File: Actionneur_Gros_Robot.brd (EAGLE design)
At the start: 110 x 55 mm, 51 parts, among them M1 ARDUINO-NANO-3.0, M10 SERVO, M11 SERVO, M2 SERVO, M3 SERVO, M4 SERVO, M5 SERVO, M6 SERVO, M7 SERVO, M8 SERVO, M9 SERVO, Y1 16MHz

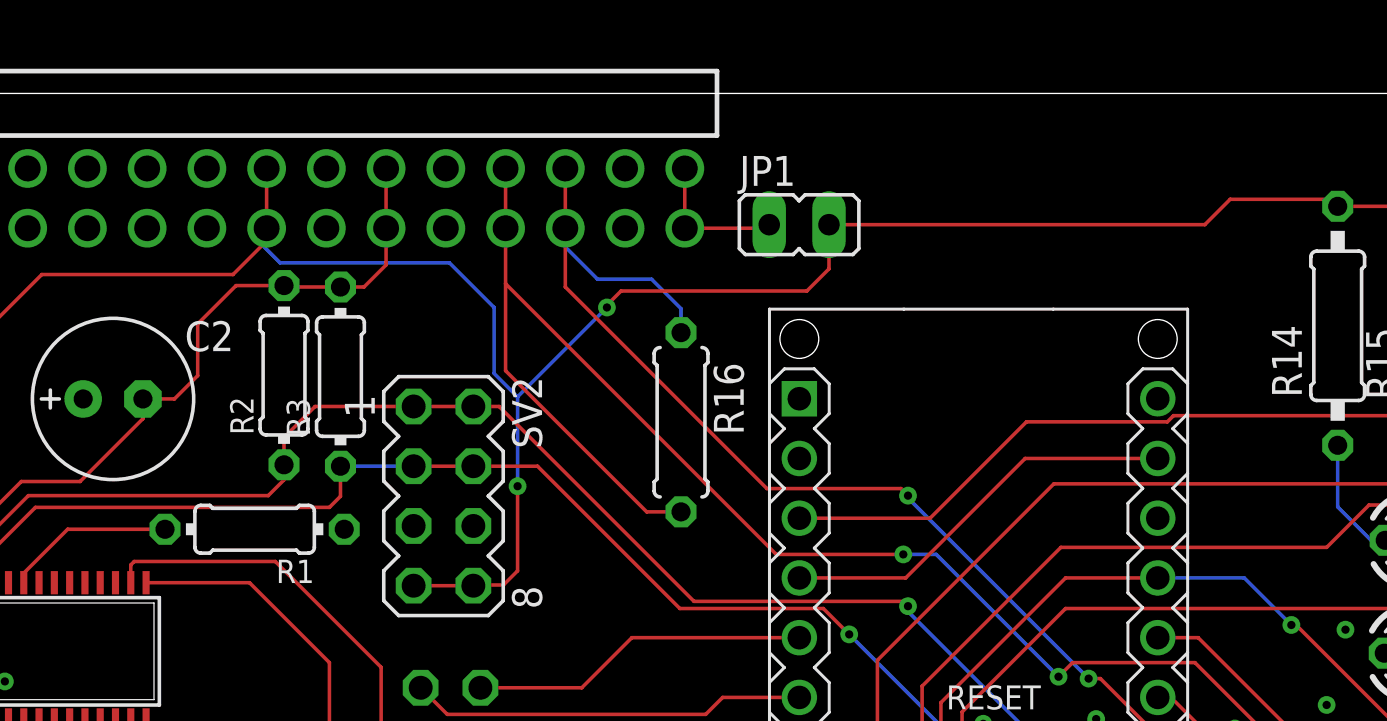
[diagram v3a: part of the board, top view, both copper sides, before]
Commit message: chgt schéma bouton d'arrêt d'urgence, condo 10 uF sur VDD
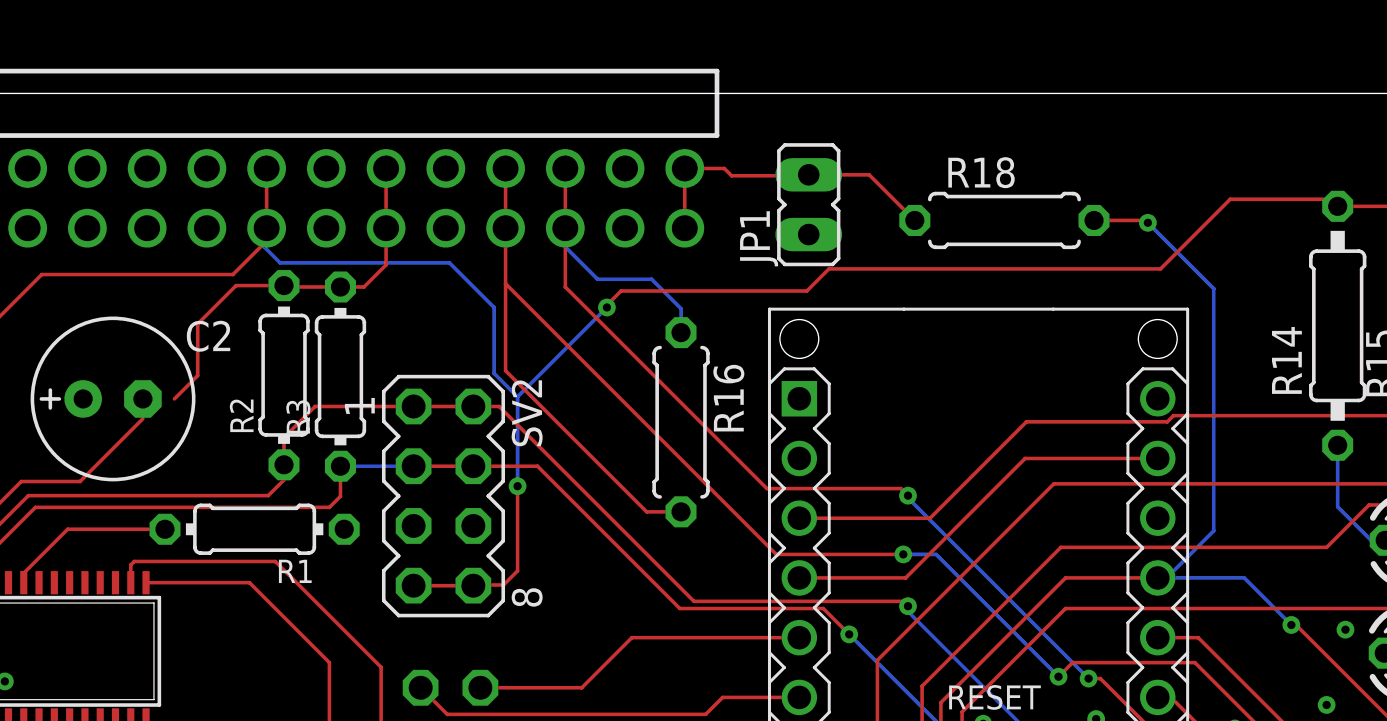
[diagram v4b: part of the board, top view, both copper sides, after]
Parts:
- added R18: 10K, rcl:0207/7
- moved JP1 0.94 mm to (50.2, 50.3), turned to 0 degrees
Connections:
- net BAU: now also JP1.2, R18.1; no longer JP1.1
- net GND: now also JP1.1
- net VCC: now also R18.2
- net VDD: no longer JP1.2
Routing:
- net VCC: track 246.5 -> 263.7 mm, vias 5 -> 6
- net BAU: track 6.19 -> 13.3 mm
- net VDD: track 189.3 -> 188.2 mm
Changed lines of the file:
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@@
 <layers>
 <layer number="1" name="Top" color="4" fill="1" visible="yes" active="yes"/>
+<layer number="2" name="Route2" color="1" fill="3" visible="no" active="no"/>
+<layer number="3" name="Route3" color="4" fill="3" visible="no" active="no"/>
+<layer number="4" name="Route4" color="1" fill="4" visible="no" active="no"/>
+<layer number="5" name="Route5" color="4" fill="4" visible="no" active="no"/>
+<layer number="6" name="Route6" color="1" fill="8" visible="no" active="no"/>
+<layer number="7" name="Route7" color="4" fill="8" visible="no" active="no"/>
+<layer number="8" name="Route8" color="1" fill="2" visible="no" active="no"/>
+<layer number="9" name="Route9" color="4" fill="2" visible="no" active="no"/>
+<layer number="10" name="Route10" color="1" fill="7" visible="no" active="no"/>
+<layer number="11" name="Route11" color="4" fill="7" visible="no" active="no"/>
+<layer number="12" name="Route12" color="1" fill="5" visible="no" active="no"/>
+<layer number="13" name="Route13" color="4" fill="5" visible="no" active="no"/>
+<layer number="14" name="Route14" color="1" fill="6" visible="no" active="no"/>
+<layer number="15" name="Route15" color="4" fill="6" visible="no" active="no"/>
 <layer number="16" name="Bottom" color="1" fill="1" visible="yes" active="yes"/>
 <layer number="17" name="Pads" color="2" fill="1" visible="yes" active="yes"/>
@@
 <attribute name="VALUE" x="4.7052" y="55.5702" size="0.8128" layer="27" rot="R180"/>
 </element>
-<element name="JP1" library="jumper" library_urn="urn:adsk.eagle:library:252" package="JP1" package3d_urn="urn:adsk.eagle:package:15455/1" value="" x="49.77" y="49.42" smashed="yes" rot="R270">
-<attribute name="NAME" x="47.23" y="51.071" size="1.27" layer="25" ratio="10"/>
-<attribute name="POPULARITY" value="61" x="-15" y="29.1" size="1.778" layer="27" rot="R270" display="off"/>
-<attribute name="VALUE" x="47.23" y="46.499" size="1.27" layer="27" ratio="10"/>
+<element name="JP1" library="jumper" library_urn="urn:adsk.eagle:library:252" package="JP1" package3d_urn="urn:adsk.eagle:package:15455/1" value="" x="50.18" y="50.27" smashed="yes">
+<attribute name="NAME" x="48.529" y="47.73" size="1.27" layer="25" ratio="10" rot="R90"/>
+<attribute name="POPULARITY" value="61" x="70.5" y="-14.5" size="1.778" layer="27" display="off"/>
+<attribute name="VALUE" x="53.101" y="47.73" size="1.27" layer="27" ratio="10" rot="R90"/>
 </element>
 <element name="LED1" library="led" library_urn="urn:adsk.eagle:library:259" package="LED3MM" package3d_urn="urn:adsk.eagle:package:15797/1" value="" x="75.92" y="31.2" smashed="yes">
@@
 <attribute name="POPULARITY" value="15" x="4.6" y="42.3" size="1.778" layer="27" rot="R90" display="off"/>
 <attribute name="VALUE" x="8.791" y="41.03" size="1.27" layer="27" ratio="10" rot="R90"/>
+</element>
+<element name="R18" library="rcl" library_urn="urn:adsk.eagle:library:334" package="0207/7" package3d_urn="urn:adsk.eagle:package:23493/2" value="10K" x="58.5" y="49.6" smashed="yes">
+<attribute name="NAME" x="55.96" y="50.997" size="1.27" layer="25" ratio="10"/>
+<attribute name="POPULARITY" value="46" x="58.5" y="49.6" size="1.778" layer="27" display="off"/>
+<attribute name="SPICEPREFIX" value="R" x="58.5" y="49.6" size="1.778" layer="27" display="off"/>
+<attribute name="VALUE" x="56.214" y="49.0412" size="1.27" layer="27" ratio="10"/>
 </element>
 </elements>
@@
 <contactref element="SV5" pad="3"/>
 <contactref element="SV5" pad="1"/>
+<contactref element="JP1" pad="1"/>
 </signal>
 <signal name="N$1">
@@
 <contactref element="M11" pad="2"/>
 <contactref element="R4" pad="2"/>
-<contactref element="C2" pad="-"/>
 <contactref element="R5" pad="2"/>
 <contactref element="R6" pad="2"/>
@@
 <via x="70.7" y="32.4" extent="1-16" drill="0.35"/>
 <wire x1="70.7" y1="32.4" x2="68.7" y2="34.4" width="0.1524" layer="16"/>
-<wire x1="68.7" y1="34.4" x2="65.02" y2="34.4" width="0.1524" layer="16"/>
+<wire x1="68.7" y1="34.4" x2="65.4" y2="34.4" width="0.1524" layer="16"/>
+<wire x1="65.3" y1="34.4" x2="65.02" y2="34.4" width="0.1524" layer="16"/>
 <wire x1="39.32" y1="4.93" x2="35.33" y2="4.93" width="0.1524" layer="1"/>
 <wire x1="35.33" y1="4.93" x2="35.32" y2="4.94" width="0.1524" layer="1"/>
@@
 <wire x1="24.2" y1="45.2" x2="24.2" y2="43" width="0.1524" layer="1"/>
 <wire x1="24.2" y1="43" x2="23.21" y2="42.01" width="0.1524" layer="1"/>
-<wire x1="23.21" y1="42.01" x2="21.87" y2="42.01" width="0.1524" layer="1"/>
 <wire x1="25.83" y1="46.83" x2="24.2" y2="45.2" width="0.1524" layer="1"/>
-<wire x1="21.87" y1="42.01" x2="21.87" y2="41.17" width="0.1524" layer="1"/>
 <wire x1="19.2" y1="38.5" x2="16.7" y2="38.5" width="0.1524" layer="1"/>
 <wire x1="16.7" y1="38.5" x2="13.555" y2="35.355" width="0.1524" layer="1"/>
@@
 <wire x1="16" y1="27.4" x2="16.155" y2="27.555" width="0.1524" layer="1"/>
 <wire x1="16.155" y1="27.555" x2="16.155" y2="28.3622" width="0.1524" layer="1"/>
+<contactref element="C2" pad="-"/>
+<contactref element="R18" pad="2"/>
+<wire x1="62.31" y1="49.6" x2="64.5" y2="49.6" width="0.1524" layer="1"/>
+<wire x1="64.5" y1="49.6" x2="64.6" y2="49.5" width="0.1524" layer="1"/>
+<via x="64.6" y="49.5" extent="1-16" drill="0.35"/>
+<wire x1="64.6" y1="49.5" x2="67.4" y2="46.7" width="0.1524" layer="16"/>
+<wire x1="67.4" y1="46.7" x2="67.4" y2="36.4" width="0.1524" layer="16"/>
+<wire x1="67.4" y1="36.4" x2="65.4" y2="34.4" width="0.1524" layer="16"/>
+<wire x1="65.4" y1="34.4" x2="65.3" y2="34.4" width="0.1524" layer="16"/>
+<wire x1="21.87" y1="42.01" x2="23.21" y2="42.01" width="0" layer="19" extent="1-1"/>
+<wire x1="21.87" y1="41.17" x2="21.87" y2="42.01" width="0" layer="19" extent="1-1"/>
 </signal>
 <signal name="I2C_SDA">
@@
 <contactref element="LED3" pad="K"/>
 <contactref element="U$3" pad="18"/>
-<contactref element="JP1" pad="2"/>
 <contactref element="SV1" pad="8"/>
 <contactref element="SV1" pad="7"/>
@@
 <wire x1="72.67" y1="50.2" x2="76.57" y2="50.2" width="0.1524" layer="1"/>
 <wire x1="76.57" y1="50.2" x2="76.67" y2="50.1" width="0.1524" layer="1"/>
-<wire x1="51.04" y1="49.42" x2="67.02" y2="49.42" width="0.1524" layer="1"/>
-<wire x1="67.02" y1="49.42" x2="68.1" y2="50.5" width="0.1524" layer="1"/>
 <wire x1="68.1" y1="50.5" x2="72.37" y2="50.5" width="0.1524" layer="1"/>
 <wire x1="72.37" y1="50.5" x2="72.67" y2="50.2" width="0.1524" layer="1"/>
@@
 <wire x1="84.51" y1="41.89" x2="86.5932" y2="39.8068" width="0.1524" layer="1"/>
 <wire x1="33.38" y1="34.07" x2="35.92" y2="34.07" width="0.1524" layer="1"/>
-<wire x1="51.04" y1="49.42" x2="51.04" y2="47.54" width="0.1524" layer="1"/>
 <wire x1="50.1" y1="46.6" x2="42.2" y2="46.6" width="0.1524" layer="1"/>
 <wire x1="42.2" y1="46.6" x2="41.6" y2="46" width="0.1524" layer="1"/>
@@
 <wire x1="37.2" y1="34.1" x2="35.95" y2="34.1" width="0.1524" layer="1"/>
 <wire x1="35.92" y1="34.07" x2="35.95" y2="34.1" width="0.1524" layer="1"/>
-<wire x1="51.04" y1="47.54" x2="50.1" y2="46.6" width="0.1524" layer="1"/>
+<wire x1="50.1" y1="46.6" x2="51.04" y2="47.54" width="0.1524" layer="1"/>
 <wire x1="37.8" y1="42.1" x2="36.8" y2="43.1" width="0.1524" layer="16"/>
 <wire x1="36.8" y1="43.1" x2="36.8" y2="45.9" width="0.1524" layer="16"/>
@@
 <wire x1="27.13" y1="48.73" x2="27.13" y2="49.27" width="0.1524" layer="1"/>
 <wire x1="17.57" y1="47.3" x2="25.7" y2="47.3" width="0.1524" layer="1"/>
+<wire x1="51.04" y1="47.54" x2="65.14" y2="47.54" width="0.1524" layer="1"/>
+<wire x1="65.14" y1="47.54" x2="68.1" y2="50.5" width="0.1524" layer="1"/>
 </signal>
 <signal name="N$16">
@@
 <contactref element="J3" pad="32"/>
 <contactref element="J3" pad="31"/>
-<contactref element="JP1" pad="1"/>
-<wire x1="48.5" y1="49.42" x2="48.35" y2="49.27" width="0.1524" layer="1"/>
-<wire x1="48.35" y1="49.27" x2="44.91" y2="49.27" width="0.1524" layer="1"/>
 <wire x1="44.91" y1="51.81" x2="44.91" y2="49.27" width="0.1524" layer="1"/>
+<contactref element="JP1" pad="2"/>
+<contactref element="R18" pad="1"/>
+<wire x1="54.69" y1="49.6" x2="52.75" y2="51.54" width="0.1524" layer="1"/>
+<wire x1="52.75" y1="51.54" x2="50.18" y2="51.54" width="0.1524" layer="1"/>
+<wire x1="44.91" y1="51.81" x2="46.59" y2="51.81" width="0.1524" layer="1"/>
+<wire x1="46.59" y1="51.81" x2="46.9" y2="51.5" width="0.1524" layer="1"/>
+<wire x1="46.9" y1="51.5" x2="50.14" y2="51.5" width="0.1524" layer="1"/>
+<wire x1="50.14" y1="51.5" x2="50.18" y2="51.54" width="0.1524" layer="1"/>
 </signal>
 <signal name="+12V">

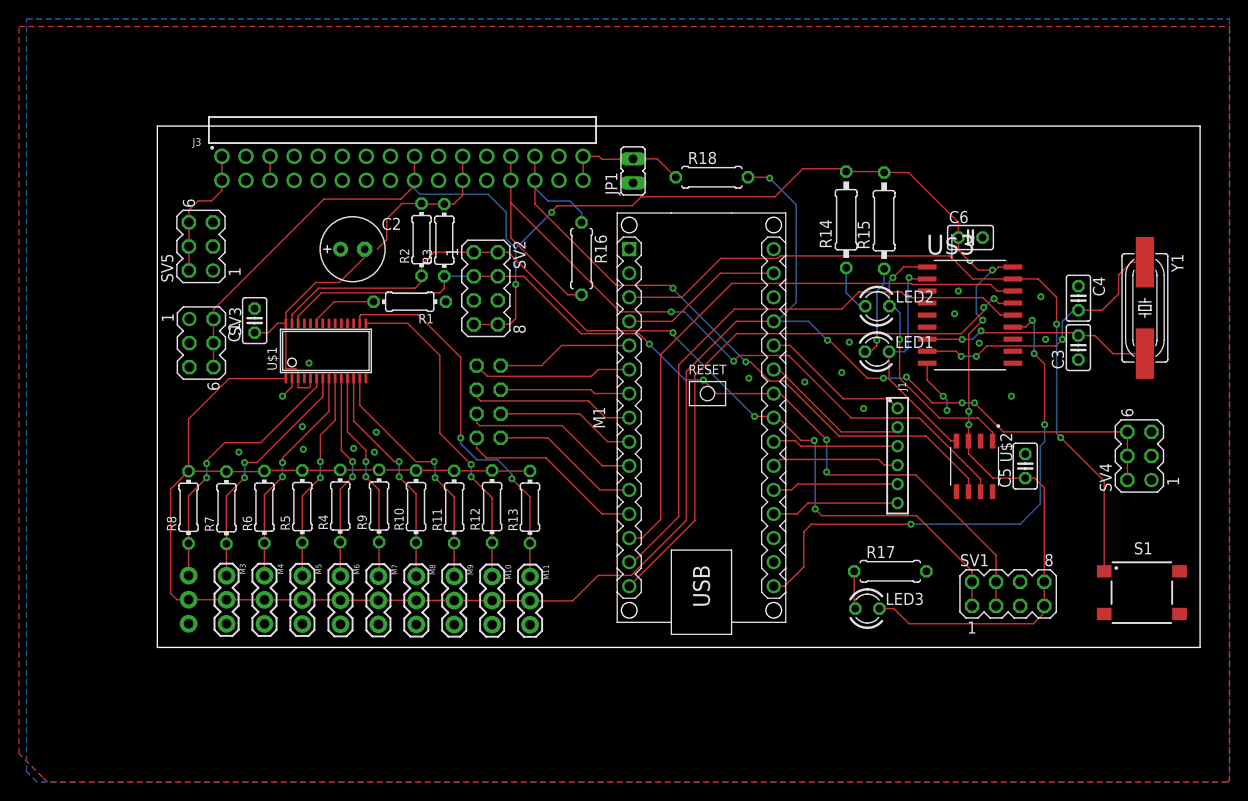
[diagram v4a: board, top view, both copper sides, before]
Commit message: Added CAM job
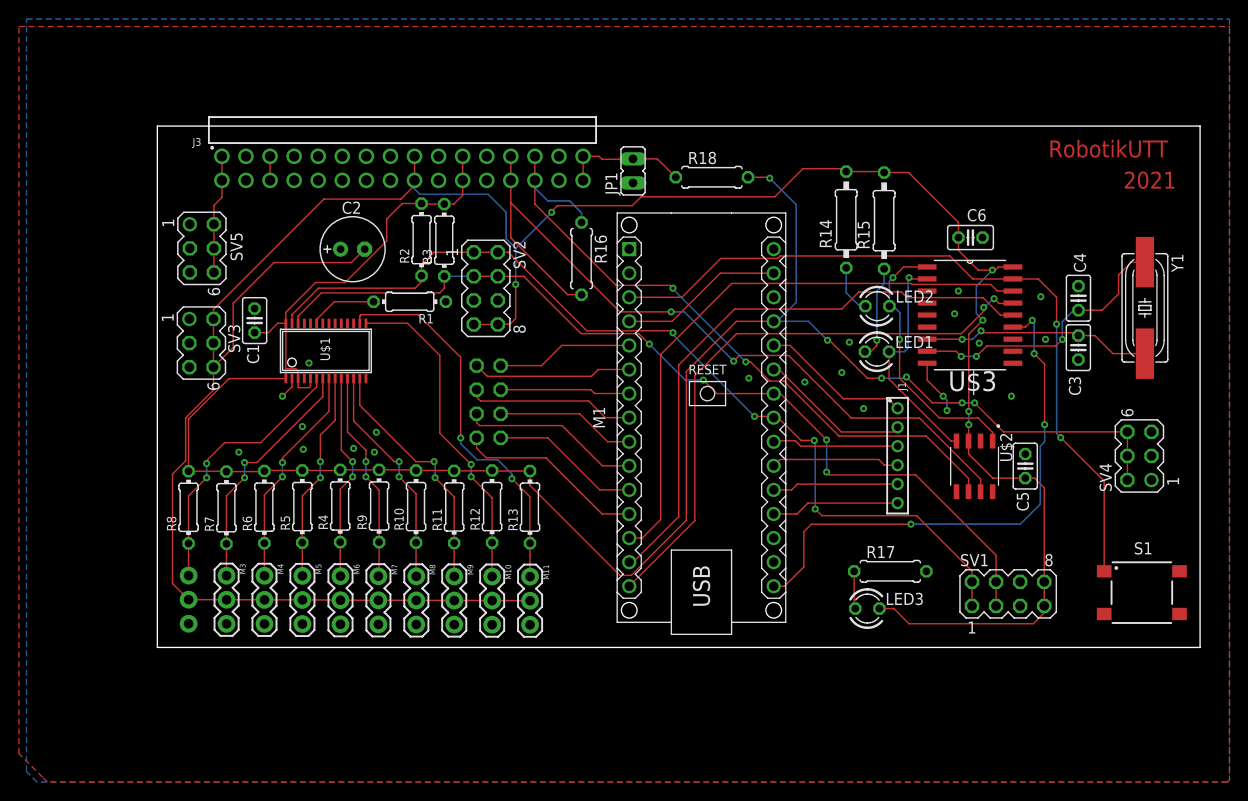
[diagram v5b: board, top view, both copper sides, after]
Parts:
- moved SV5 0.22 mm to (4.70, 42.1), turned to 270 degrees
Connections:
- net VCC: no longer C2.-, M10.2, M11.2, M2.2, M3.2, M4.2, M5.2, M6.2, M7.2, M8.2, M9.2
- net VDD: now also C2.-, M10.2, M11.2, M2.2, M3.2, M4.2, M5.2, M6.2, M7.2, M8.2, M9.2
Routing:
- net VDD: track 188.2 -> 275.2 mm
- net VCC: track 263.7 -> 217.4 mm
- net +12V: track 14.3 -> 12.6 mm
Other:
- board text added: "2021"
- board text added: "RobotikUTT"

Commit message: ajout des fichiers gerber
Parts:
- moved J2 3.50 mm to (38.5, 25.8)
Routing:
- net N$8: track 20.1 -> 15.9 mm
- net N$10: track 18.9 -> 14.8 mm
- net N$12: track 17.8 -> 13.8 mm
- net IRQ1: track 16.9 -> 13.3 mm
- net N$13: track 13.7 -> 10.2 mm
- net N$11: track 14.8 -> 11.2 mm
- net N$9: track 15.8 -> 12.3 mm
- net IRQ0: track 14.4 -> 11.0 mm
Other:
- board text added: "ROBOTIK UTT 2021"
- board text removed: "2021"
- board text removed: "RobotikUTT"

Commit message: revA02
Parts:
- C2: value 10uF -> 47uF
- R2: value (none) -> 10k
- moved C2 0.22 mm to (20.4, 42.1), turned to 180 degrees
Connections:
- net GND: now also C2.-; no longer C2.+
- net VDD: now also C2.+; no longer C2.-
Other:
- board text added: "Viet Phuong DINH"
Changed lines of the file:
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@@
 <layer number="24" name="bOrigins" color="15" fill="1" visible="yes" active="yes"/>
 <layer number="25" name="tNames" color="7" fill="1" visible="yes" active="yes"/>
-<layer number="26" name="bNames" color="7" fill="1" visible="yes" active="yes"/>
+<layer number="26" name="bNames" color="7" fill="1" visible="no" active="yes"/>
 <layer number="27" name="tValues" color="7" fill="1" visible="yes" active="yes"/>
 <layer number="28" name="bValues" color="7" fill="1" visible="yes" active="yes"/>
@@
 </polygon>
 <text x="32.7" y="43.8" size="1.778" layer="26" font="vector" rot="MR0">ROBOTIK UTT 2021</text>
+<text x="31.9" y="40" size="1.778" layer="26" rot="MR0">Viet Phuong DINH</text>
 </plain>
 <attributes>
@@
 <attribute name="VALUE" x="13.054" y="34.494" size="1.27" layer="27" ratio="10" rot="R90"/>
 </element>
-<element name="C2" library="rcl" library_urn="urn:adsk.eagle:library:334" package="E2,5-7" package3d_urn="urn:adsk.eagle:package:23345/1" value="10uF" x="20.6" y="42.01" smashed="yes">
-<attribute name="NAME" x="19.448" y="45.742" size="1.27" layer="25" ratio="10"/>
-<attribute name="POPULARITY" value="17" x="71.4" y="-12.6" size="1.778" layer="27" display="off"/>
-<attribute name="SPICEPREFIX" value="C" x="71.4" y="-12.6" size="1.778" layer="27" display="off"/>
-<attribute name="VALUE" x="18.448" y="43.735" size="1.27" layer="27" ratio="10"/>
+<element name="C2" library="rcl" library_urn="urn:adsk.eagle:library:334" package="E2,5-7" package3d_urn="urn:adsk.eagle:package:23345/1" value="47uF" x="20.4" y="42.09" smashed="yes" rot="R180">
+<attribute name="NAME" x="21.552" y="38.358" size="1.27" layer="25" ratio="10" rot="R180"/>
+<attribute name="POPULARITY" value="17" x="-30.4" y="96.7" size="1.778" layer="27" rot="R180" display="off"/>
+<attribute name="SPICEPREFIX" value="C" x="-30.4" y="96.7" size="1.778" layer="27" rot="R180" display="off"/>
+<attribute name="VALUE" x="22.552" y="40.365" size="1.27" layer="27" ratio="10" rot="R180"/>
 </element>
 <element name="C3" library="rcl" library_urn="urn:adsk.eagle:library:334" package="C025-025X050" package3d_urn="urn:adsk.eagle:package:23629/2" value="22pF" x="97.16" y="31.63" smashed="yes" rot="R90">
@@
 <attribute name="VALUE" x="75.034" y="7.4712" size="1.27" layer="27" ratio="10"/>
 </element>
-<element name="R2" library="rcl" library_urn="urn:adsk.eagle:library:334" package="0204/7" package3d_urn="urn:adsk.eagle:package:23498/2" value="" x="27.87" y="43.02" smashed="yes" rot="R90">
+<element name="R2" library="rcl" library_urn="urn:adsk.eagle:library:334" package="0204/7" package3d_urn="urn:adsk.eagle:package:23498/2" value="10k" x="27.87" y="43.02" smashed="yes" rot="R90">
 <attribute name="NAME" x="26.5746" y="40.48" size="0.9906" layer="25" ratio="10" rot="R90"/>
 <attribute name="POPULARITY" value="79" x="102.8" y="111.6" size="1.778" layer="27" rot="R90" display="off"/>
@@
 <contactref element="S1" pad="2"/>
 <contactref element="S1" pad="4"/>
-<contactref element="C2" pad="+"/>
 <contactref element="U$2" pad="2"/>
 <contactref element="C4" pad="1"/>
@@
 <contactref element="SV5" pad="1"/>
 <contactref element="JP1" pad="1"/>
+<contactref element="C2" pad="-"/>
 </signal>
 <signal name="N$1">
@@
 <wire x1="51.04" y1="47.54" x2="65.14" y2="47.54" width="0.1524" layer="1"/>
 <wire x1="65.14" y1="47.54" x2="68.1" y2="50.5" width="0.1524" layer="1"/>
-<contactref element="C2" pad="-"/>
 <contactref element="M2" pad="2"/>
 <contactref element="M3" pad="2"/>
@@
 <contactref element="M11" pad="2"/>
 <wire x1="5.92" y1="29.57" x2="8" y2="31.65" width="0.1524" layer="1"/>
-<wire x1="20.46" y1="40.6" x2="21.87" y2="42.01" width="0.1524" layer="1"/>
 <wire x1="8" y1="31.65" x2="8" y2="36.3" width="0.1524" layer="1"/>
 <wire x1="8" y1="36.3" x2="12.3" y2="40.6" width="0.1524" layer="1"/>
-<wire x1="12.3" y1="40.6" x2="20.46" y2="40.6" width="0.1524" layer="1"/>
 <wire x1="5.92" y1="29.57" x2="5.92" y2="27.15105625" width="0.1524" layer="1"/>
 <wire x1="5.92" y1="27.15105625" x2="2.9852" y2="24.21625625" width="0.1524" layer="1"/>
@@
 <wire x1="35.32" y1="4.94" x2="39.31" y2="4.94" width="0.1524" layer="1"/>
 <wire x1="39.31" y1="4.94" x2="39.32" y2="4.93" width="0.1524" layer="1"/>
+<contactref element="C2" pad="+"/>
+<wire x1="20.18" y1="40.6" x2="21.67" y2="42.09" width="0.1524" layer="1"/>
+<wire x1="12.3" y1="40.6" x2="20.18" y2="40.6" width="0.1524" layer="1"/>
 </signal>
 <signal name="N$16">
